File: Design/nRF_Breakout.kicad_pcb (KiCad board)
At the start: 2 copper layers, 26 x 51 mm, 14 parts, among them IC1 LM1117, P1 CONN_01X18, P10 CONN_01X01, P2 CONN_01X08, P3 CONN_01X18, P5 CONN_01X08, P7 CONN_01X01, P8 CONN_01X01, P9 CONN_01X01, U1 nRF51822

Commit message: ADDED NEW FILES
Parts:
- added C1: 10uF, Capacitors_SMD:C_1206_HandSoldering, B.Cu at (179.8, 97.2)
- added C2: 0.1uF, Capacitors_SMD:C_0603_HandSoldering, B.Cu at (166.5, 97.2)
- added P4: CONN_01X02, Pin_Headers:Pin_Header_Straight_1x02, F.Cu at (184.2, 92.5)
- IC1: moved to B.Cu
- moved IC1 32.7 mm to (173.0, 97.3), turned to 270 degrees
- moved P10 8.45 mm to (162.7, 99.9)
- moved P7 8.33 mm to (185.3, 99.8)
- moved D2 1.28 mm to (177.5, 43.8)
- moved D1 0.64 mm to (170.2, 43.8)
- moved P5 0.49 mm to (184.2, 69.8)
- moved P2 0.48 mm to (163.8, 69.8)
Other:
- board size 26 x 51 mm -> 26 x 59 mm
- board text added: "3.3V"
- board text added: "GND"
- board text added: "P0.00"
- board text added: "P0.01"
- board text added: "P0.02"
- board text added: "P0.03"
- board text added: "P0.04"
- board text added: "P0.05"
- board text added: "P0.06"
- board text added: "P0.07"
- board text added: "P0.08"
- board text added: "P0.09"
- board text added: "P0.10"
- board text added: "P0.11"
- board text added: "P0.12"
- board text added: "P0.13"
- board text added: "P0.14"
- board text added: "P0.15"
- board text added: "P0.17"
- board text added: "P0.18"
- board text added: "P0.19"
- board text added: "P0.20"
- board text added: "P0.21"
- board text added: "P0.22"
- board text added: "P0.23"
- board text added: "P0.24"
- board text added: "P0.25"
- board text added: "P0.26"
- board text added: "P0.27"
- board text added: "P0.28"
- board text added: "P0.29"
- board text added: "P0.30"
- board text added: "P016"
- board text added: "SWD"
- board text added: "SWDIO"
- board text added: "pwr"
- board text added: "status"
- board text removed: "p0.11"

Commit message: Corrected File
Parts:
- removed D2: LED, ee:LED-0603_NEW
- removed P10, P9: CONN_01X01, Connect:1pin
- removed R2: 470r, Resistors_SMD:R_0603_HandSoldering
- added P6: CONN_01X02, Pin_Headers:Pin_Header_Straight_1x02, F.Cu at (163.5, 96.0)
- moved D1 24.3 mm to (164.6, 67.4)
- moved R1 24.2 mm to (164.0, 69.3), turned to 180 degrees
- moved P8 19.7 mm to (174.0, 60.5)
- moved P7 17.8 mm to (174.0, 86.0)
- moved P4 3.56 mm to (184.5, 96.0)
- moved P2 2.54 mm to (163.8, 72.4)
- moved P5 2.54 mm to (184.2, 72.4)
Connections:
- net +3.3VP renamed Net-(C2-Pad1)
- net ST_LED renamed Net-(P1-Pad2)
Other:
- board size 26 x 59 mm -> 26 x 55.5 mm
- board text added: "+5V"
- board text added: "P00"
- board text added: "P01"
- board text added: "P02"
- board text added: "P03"
- board text added: "P04"
- board text added: "P05"
- board text added: "P06"
- board text added: "P07"
- board text added: "P08"
- board text added: "P09"
- board text added: "P10"
- board text added: "P11"
- board text added: "P12"
- board text added: "P13"
- board text added: "P14"
- board text added: "P15"
- board text added: "P16"
- board text added: "P17"
- board text added: "P18"
- board text added: "P19"
- board text added: "P20"
- board text added: "P21"
- board text added: "P22"
- board text added: "P23"
- board text added: "P24"
- board text added: "P25"
- board text added: "P26"
- board text added: "P27"
- board text added: "P28"
- board text added: "P29"
- board text added: "P30"
- board text added: "STS"
- board text removed: "P0.00"
- board text removed: "P0.01"
- board text removed: "P0.02"
- board text removed: "P0.03"
- board text removed: "P0.04"
- board text removed: "P0.05"
- board text removed: "P0.06"
- board text removed: "P0.07"
- board text removed: "P0.08"
- board text removed: "P0.09"
- board text removed: "P0.10"
- board text removed: "P0.11"
- board text removed: "P0.12"
- board text removed: "P0.13"
- board text removed: "P0.14"
- board text removed: "P0.15"
- board text removed: "P0.17"
- board text removed: "P0.18"
- board text removed: "P0.19"
- board text removed: "P0.20"
- board text removed: "P0.21"
- board text removed: "P0.22"
- board text removed: "P0.23"
- board text removed: "P0.24"
- board text removed: "P0.25"
- board text removed: "P0.26"
- board text removed: "P0.27"
- board text removed: "P0.28"
- board text removed: "P0.29"
- board text removed: "P0.30"
- board text removed: "P016"
- board text removed: "pwr"
- board text removed: "status"

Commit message: corrected files
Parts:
- turned D1 to 180 degrees
- turned R1 to 0 degrees
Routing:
- net GND: track 0.00 -> 95.0 mm, vias 0 -> 1
- net Net-(P3-Pad5): track 0.00 -> 70.7 mm, vias 0 -> 1
- net Net-(P3-Pad6): track 0.00 -> 63.0 mm, vias 0 -> 1
- net Net-(C2-Pad1): track 0.00 -> 58.8 mm, vias 0 -> 1
- net Net-(P1-Pad2): track 0.00 -> 33.1 mm
- net Net-(P3-Pad17): track 0.00 -> 32.0 mm
- net Net-(P1-Pad17): track 0.00 -> 31.1 mm
- net Net-(P3-Pad18): track 0.00 -> 30.6 mm
- net Net-(P1-Pad18): track 0.00 -> 29.4 mm
- net Net-(P3-Pad15): track 0.00 -> 28.4 mm
- net Net-(P1-Pad15): track 0.00 -> 28.2 mm
- net Net-(P3-Pad16): track 0.00 -> 27.5 mm
- net Net-(P1-Pad16): track 0.00 -> 26.9 mm
- net Net-(P3-Pad13): track 0.00 -> 25.4 mm
- net Net-(P1-Pad13): track 0.00 -> 25.1 mm
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- added copper zone on B.Cu, net GND
- added copper zone on F.Cu, net Net-(C2-Pad1)
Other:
- outline, holes or cut-outs redrawn
- net class Default: clearance 0.254 -> 0.1778
- rule trace_clearance: 0.254 -> 0.1778
- board text added: "00"
- board text added: "01"
- board text added: "02"
- board text added: "03"
- board text added: "04"
- board text added: "05"
- board text added: "06"
- board text added: "07"
- board text added: "08"
- board text added: "09"
- board text added: "10"
- board text added: "11"
- board text added: "12"
- board text added: "13"
- board text added: "14"
- board text added: "15"
- board text added: "16"
- board text added: "17"
- board text added: "18"
- board text added: "19"
- board text added: "20"
- board text added: "21"
- board text added: "22"
- board text added: "23"
- board text added: "24"
- board text added: "25"
- board text added: "26"
- board text added: "27"
- board text added: "28"
- board text added: "29"
- board text added: "30"
- board text removed: "P00"
- board text removed: "P01"
- board text removed: "P02"
- board text removed: "P03"
- board text removed: "P04"
- board text removed: "P05"
- board text removed: "P06"
- board text removed: "P07"
- board text removed: "P08"
- board text removed: "P09"
- board text removed: "P10"
- board text removed: "P11"
- board text removed: "P12"
- board text removed: "P13"
- board text removed: "P14"
- board text removed: "P15"
- board text removed: "P16"
- board text removed: "P17"
- board text removed: "P18"
- board text removed: "P19"
- board text removed: "P20"
- board text removed: "P21"
- board text removed: "P22"
- board text removed: "P23"
- board text removed: "P24"
- board text removed: "P25"
- board text removed: "P26"
- board text removed: "P27"
- board text removed: "P28"
- board text removed: "P29"
- board text removed: "P30"

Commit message: added logo
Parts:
- added LOGO: , logo:LOGO (2), B.Cu at (177.0, 82.7)
- added U$2: LOGO, ee:LOGO_electronut, B.Cu at (172.8, 73.0)
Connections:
- U1 pad 34: Net-(P3-Pad3) -> Net-(P3-Pad2)
- U1 pad 35: Net-(P3-Pad2) -> Net-(P3-Pad3)
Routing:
- net Net-(P3-Pad2): track 6.22 -> 8.25 mm
- net Net-(P3-Pad3): track 9.26 -> 8.72 mm
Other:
- board text added: "Electronut.in"
- board text added: "ExploreEmbedded.com"
- board text added: "SWDCK"
- board text added: "VCC"
- board text removed: "+5V"
- board text removed: "SWD"

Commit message: Changed name
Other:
- board text added: "electronut.in"
- board text added: "nRF51-E3-BO"
- board text removed: "Electronut.in"

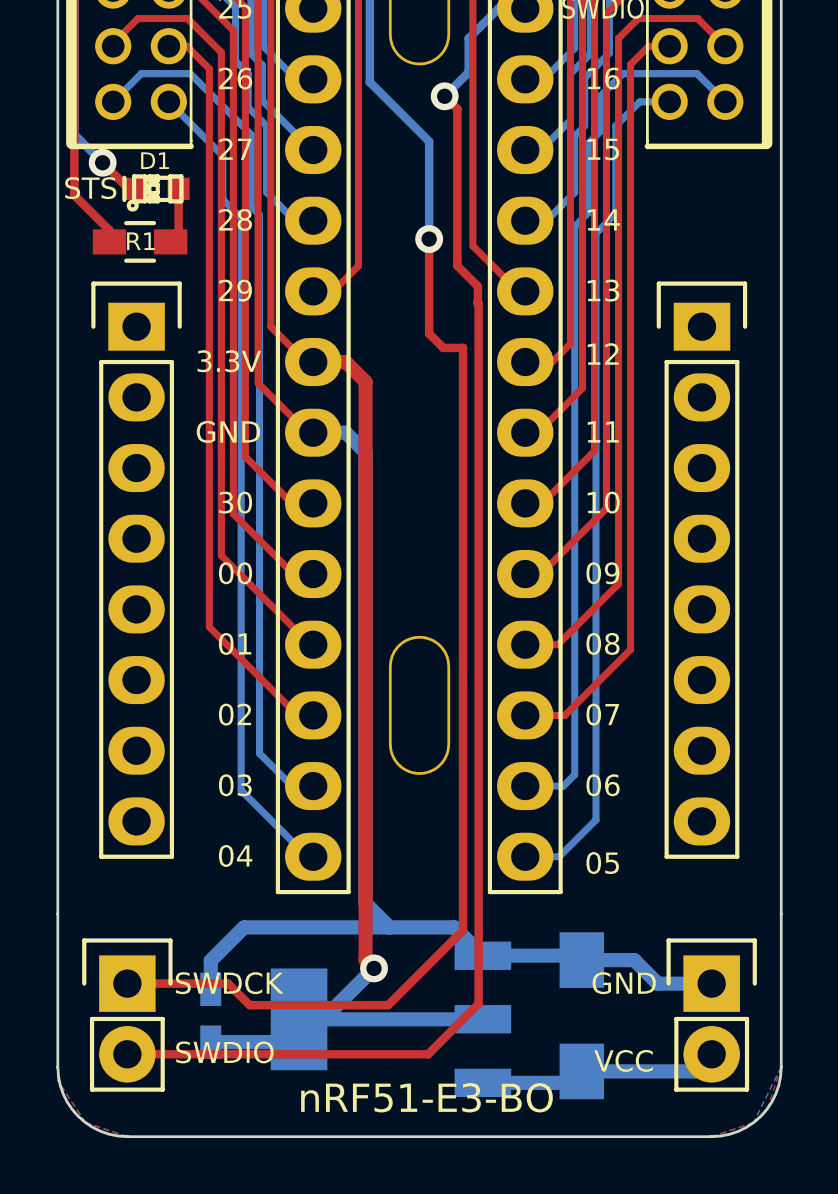
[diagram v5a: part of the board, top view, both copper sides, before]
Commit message: added board name and version
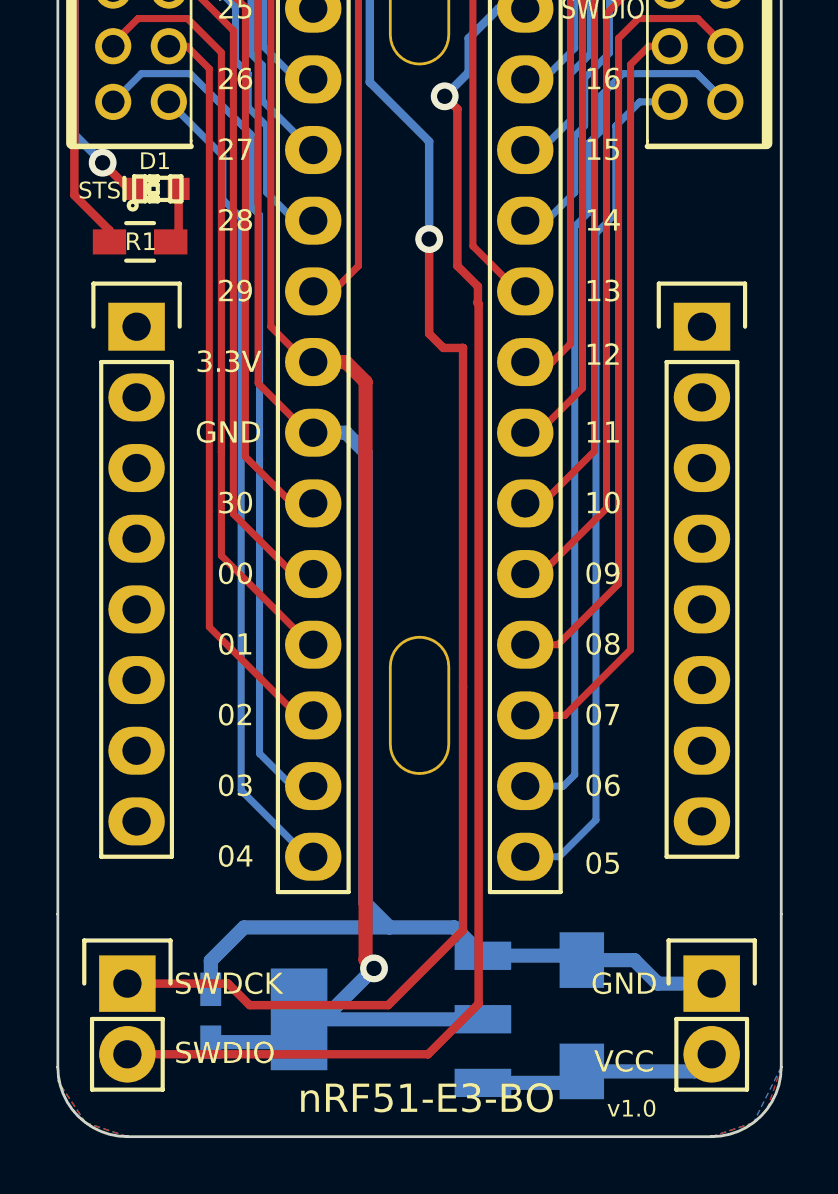
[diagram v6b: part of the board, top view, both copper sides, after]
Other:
- board text added: "v1.0"
